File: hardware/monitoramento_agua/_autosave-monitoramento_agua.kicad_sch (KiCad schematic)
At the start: 0 parts

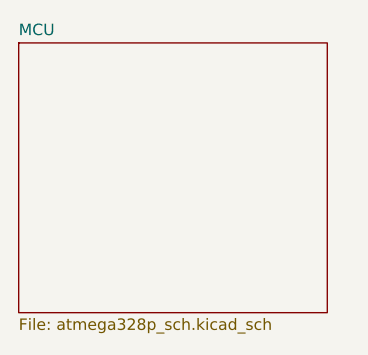
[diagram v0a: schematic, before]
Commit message: Add mcu schematic
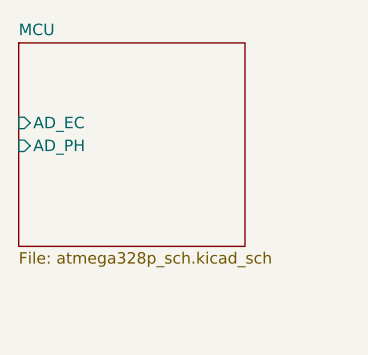
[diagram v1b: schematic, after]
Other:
- sheet MCU ports: added AD_EC, AD_PH; removed none
